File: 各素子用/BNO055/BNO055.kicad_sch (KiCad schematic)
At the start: 24 parts, among them J2 Conn_01x04_Socket, U1 LP5907MFX-2.8, U2 BNO055, Y1 Crystal

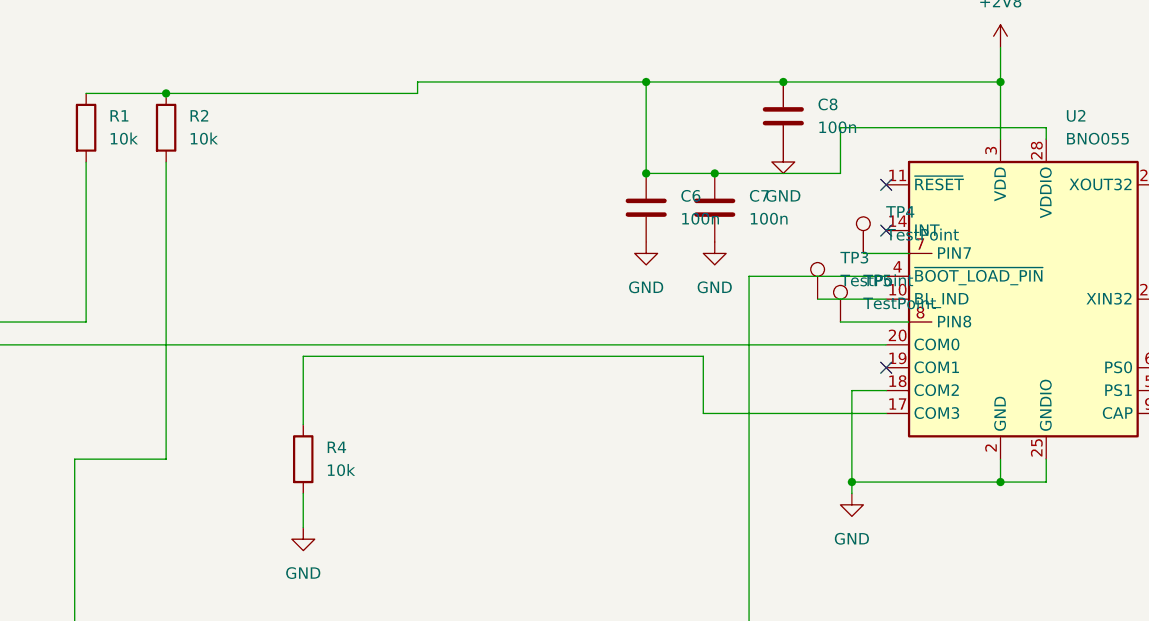
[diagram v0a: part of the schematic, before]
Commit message: RX-ESP delete
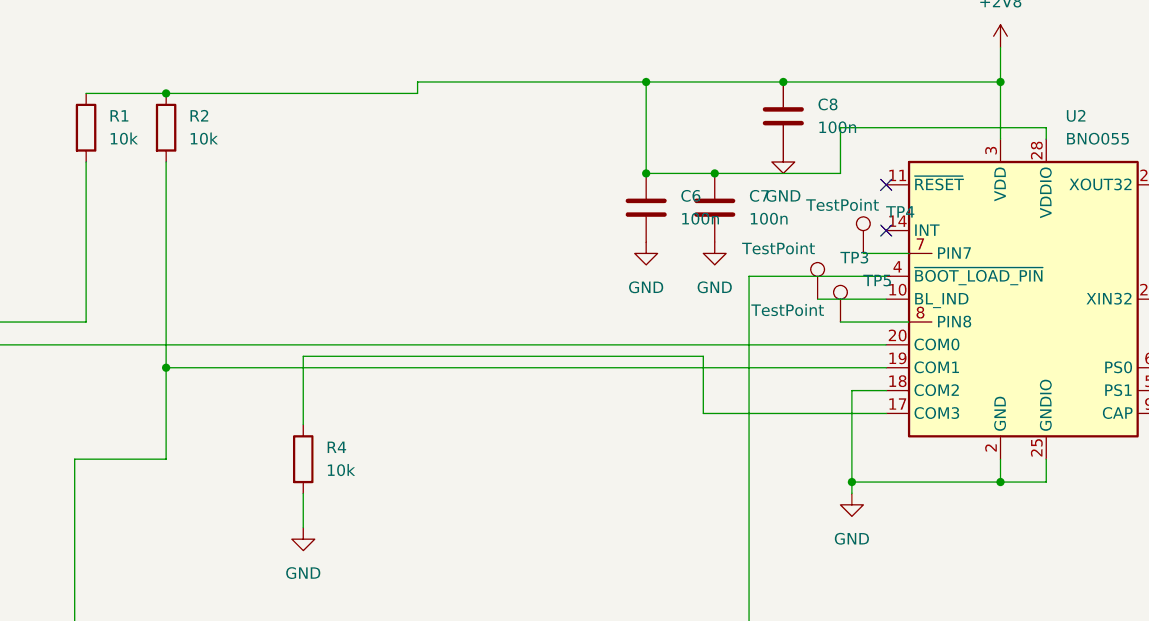
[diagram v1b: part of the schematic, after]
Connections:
- net at R2.2, U3.6 (B1): now also U2.19 (COM1)
- no-connect marks 3 -> 2
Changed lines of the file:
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@@
+	)
+	(junction
+		(at 129.54 66.04)
+		(diameter 0)
+		(color 0 0 0 0)
 	)
 	(junction
@@
 		(at 209.55 45.72)
 	)
-	(no_connect
-		(at 209.55 66.04)
-	)
 	(wire
 		(pts
@@
 	(wire
 		(pts
-			(xy 129.54 43.18) (xy 129.54 76.2)
+			(xy 129.54 43.18) (xy 129.54 66.04)
 		)
 		(stroke
@@
 	(wire
 		(pts
+			(xy 129.54 66.04) (xy 209.55 66.04)
+		)
+		(stroke
+			(width 0)
+			(type default)
+		)
+	)
+	(wire
+		(pts
 			(xy 246.38 58.42) (xy 251.46 58.42)
 		)
@@
 		(pts
 			(xy 204.47 60.96) (xy 212.09 60.96)
+		)
+		(stroke
+			(width 0)
+			(type default)
+		)
+	)
+	(wire
+		(pts
+			(xy 129.54 66.04) (xy 129.54 76.2)
 		)
 		(stroke
@@
 		(on_board yes)
 		(dnp no)
-		(fields_autoplaced yes)
 		(property "Reference" "TP5"
 			(at 207.01 56.3879 0)
@@
 		)
 		(property "Value" "TestPoint"
-			(at 207.01 58.9279 0)
+			(at 194.564 59.69 0)
 			(effects
 				(font
@@
 		(on_board yes)
 		(dnp no)
-		(fields_autoplaced yes)
 		(property "Reference" "TP3"
 			(at 204.47 53.8479 0)
@@
 		)
 		(property "Value" "TestPoint"
-			(at 204.47 56.3879 0)
+			(at 193.548 52.832 0)
 			(effects
 				(font
@@
 		(on_board yes)
 		(dnp no)
-		(fields_autoplaced yes)
 		(property "Reference" "TP4"
 			(at 209.55 48.7679 0)
@@
 		)
 		(property "Value" "TestPoint"
-			(at 209.55 51.3079 0)
-			(effects
-				(font
+			(at 200.66 48.006 0)
+			(effects
+				(font
